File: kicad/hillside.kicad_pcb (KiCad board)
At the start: 2 copper layers, 136.6 x 97.9 mm, 83 parts, among them J1 Haptic, J2 TRRS, J3 Bat_Pos, J4 Bat_GND, K1 SW_Key, K10 SW_Key, K11 SW_Key, K12 SW_Key, K13 SW_Key, K14 SW_Key, K15 SW_Key, K16 SW_Key, K17 SW_Key, K18 SW_Key, K19 SW_Key, K2 SW_Key, K20 SW_Rotary, K21 SW_Key, K22 SW_Key, K23 SW_Key, K24 SW_Key, K3 SW_Key, K4 SW_Key, K5 SW_Key, K6 SW_Key, K7 SW_Key, K8 SW_Key, K9 SW_Key, SW1 Reset, SW2 SW_Power, U1 ProMicro_r

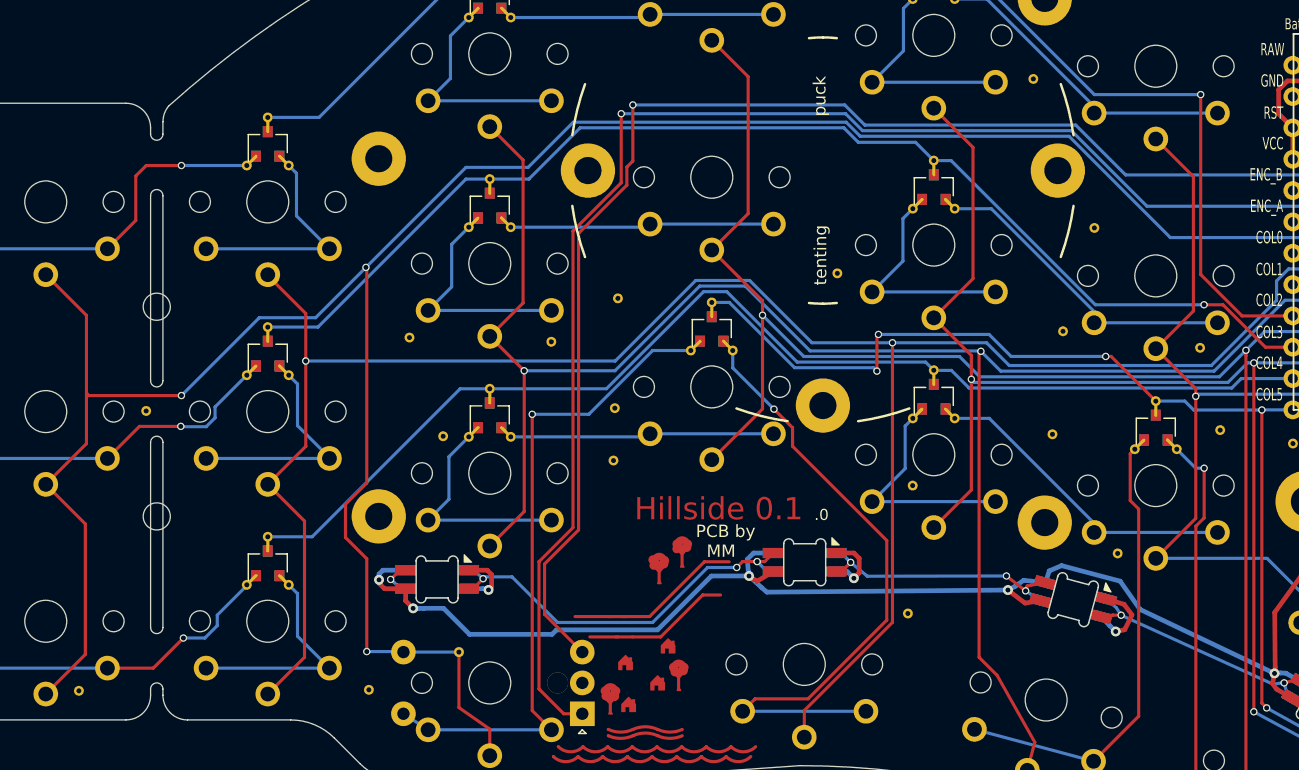
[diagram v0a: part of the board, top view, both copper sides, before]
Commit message: Remove stitching vias now handled by islands
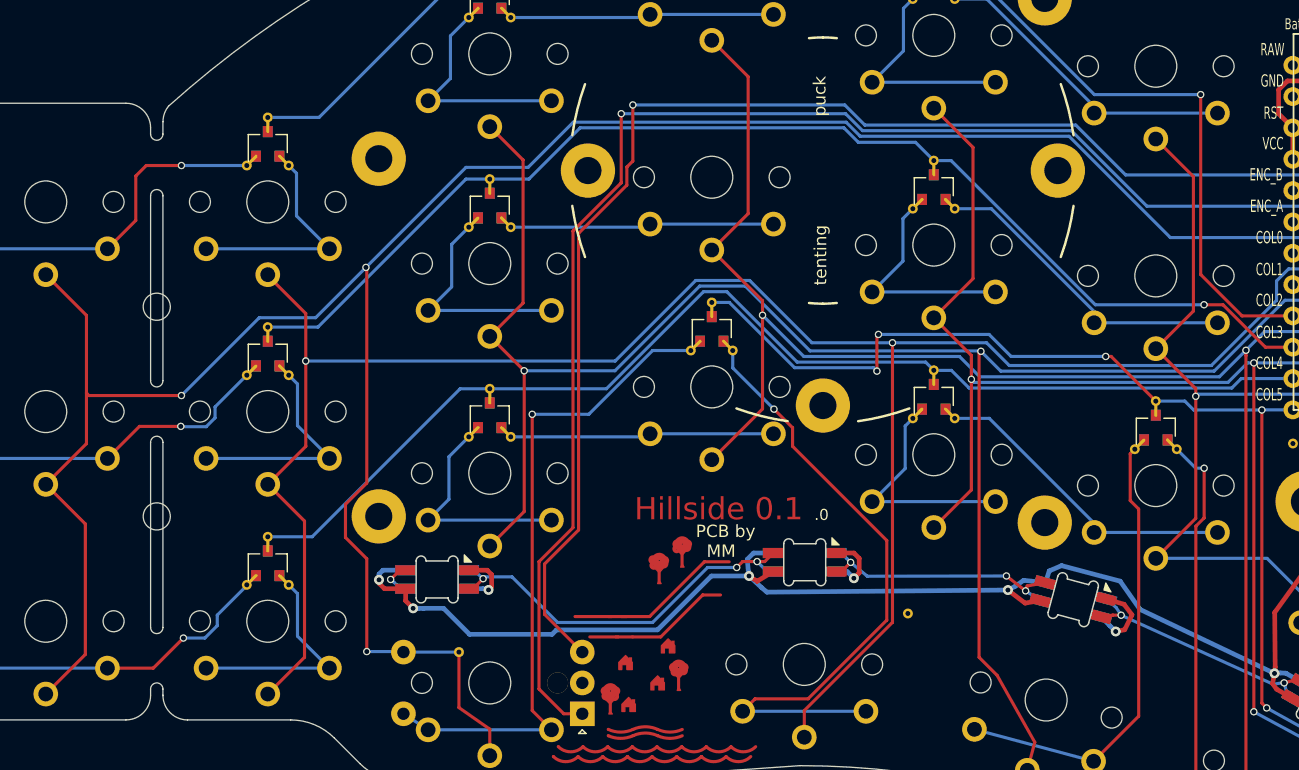
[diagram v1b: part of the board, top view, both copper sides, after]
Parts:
- removed V1, V10, V11, V12, V13, V14, V15, V16, V17, V18, V19, V20, V21, V22, V6, V7, V8, V9: Via, hillside_basic:VIA-0.8mm
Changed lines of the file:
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@@
       ))
-  )
-  (footprint "hillside_basic:VIA-0.8mm" (layer "F.Cu")
-    (at 146.03 105.47)
-    (attr through_hole)
-    (fp_text reference "V8" (at 1.3 1.4) (layer "F.Fab") hide
-      (effects (font (size 1 1) (thickness 0.15)))
-    )
-    (fp_text value "Via" (at -1.6 1.4) (layer "F.Fab") hide
-      (effects (font (size 1 1) (thickness 0.15)))
-    )
-    (pad "1" thru_hole circle locked (at 0 0) (size 0.8 0.8) (drill 0.4) (layers *.Cu)
-      (net 11 "GND") (zone_connect 2))
-  )
-  (footprint "hillside_basic:VIA-0.8mm" (layer "F.Cu")
-    (at 181.62 103.34)
-    (attr through_hole)
-    (fp_text reference "V9" (at 1.3 1.4) (layer "F.Fab") hide
-      (effects (font (size 1 1) (thickness 0.15)))
-    )
-    (fp_text value "Via" (at -1.6 1.4) (layer "F.Fab") hide
-      (effects (font (size 1 1) (thickness 0.15)))
-    )
-    (pad "1" thru_hole circle locked (at 0 0) (size 0.8 0.8) (drill 0.4) (layers *.Cu)
-      (net 11 "GND") (zone_connect 2))
-  )
-  (footprint "hillside_basic:VIA-0.8mm" (layer "F.Cu")
-    (at 126.2 124.06)
-    (attr through_hole)
-    (fp_text reference "V6" (at 1.3 1.4) (layer "F.Fab") hide
-      (effects (font (size 1 1) (thickness 0.15)))
-    )
-    (fp_text value "Via" (at -1.6 1.4) (layer "F.Fab") hide
-      (effects (font (size 1 1) (thickness 0.15)))
-    )
-    (pad "1" thru_hole circle locked (at 0 0) (size 0.8 0.8) (drill 0.4) (layers *.Cu)
-      (net 11 "GND") (zone_connect 2))
-  )
-  (footprint "hillside_basic:VIA-0.8mm" (layer "F.Cu")
-    (at 180.07 74.53)
-    (attr through_hole)
-    (fp_text reference "V1" (at 1.3 1.4) (layer "F.Fab") hide
-      (effects (font (size 1 1) (thickness 0.15)))
-    )
-    (fp_text value "Via" (at -1.6 1.4) (layer "F.Fab") hide
-      (effects (font (size 1 1) (thickness 0.15)))
-    )
-    (pad "1" thru_hole circle locked (at 0 0) (size 0.8 0.8) (drill 0.4) (layers *.Cu)
-      (net 11 "GND") (zone_connect 2))
-  )
-  (footprint "hillside_basic:VIA-0.8mm" (layer "F.Cu")
-    (at 146.39 92.32)
-    (attr through_hole)
-    (fp_text reference "V7" (at 1.3 1.4) (layer "F.Fab") hide
-      (effects (font (size 1 1) (thickness 0.15)))
-    )
-    (fp_text value "Via" (at -1.6 1.4) (layer "F.Fab") hide
-      (effects (font (size 1 1) (thickness 0.15)))
-    )
-    (pad "1" thru_hole circle locked (at 0 0) (size 0.8 0.8) (drill 0.4) (layers *.Cu)
-      (net 11 "GND") (zone_connect 2))
-  )
-  (footprint "hillside_basic:VIA-0.8mm" (layer "F.Cu")
-    (at 146.14 101.22)
-    (attr through_hole)
-    (fp_text reference "V10" (at 1.3 1.4) (layer "F.Fab") hide
-      (effects (font (size 1 1) (thickness 0.15)))
-    )
-    (fp_text value "Via" (at -1.6 1.4) (layer "F.Fab") hide
-      (effects (font (size 1 1) (thickness 0.15)))
-    )
-    (pad "1" thru_hole circle locked (at 0 0) (size 0.8 0.8) (drill 0.4) (layers *.Cu)
-      (net 11 "GND") (zone_connect 2))
-  )
-  (footprint "hillside_basic:VIA-0.8mm" (layer "F.Cu")
-    (at 182.48 94.99)
-    (attr through_hole)
-    (fp_text reference "V11" (at 1.3 1.4) (layer "F.Fab") hide
-      (effects (font (size 1 1) (thickness 0.15)))
-    )
-    (fp_text value "Via" (at -1.6 1.4) (layer "F.Fab") hide
-      (effects (font (size 1 1) (thickness 0.15)))
-    )
-    (pad "1" thru_hole circle locked (at 0 0) (size 0.8 0.8) (drill 0.4) (layers *.Cu)
-      (net 11 "GND") (zone_connect 2))
-  )
-  (footprint "hillside_basic:VIA-0.8mm" (layer "F.Cu")
-    (at 164.18 90.29)
-    (attr through_hole)
-    (fp_text reference "V12" (at 1.3 1.4) (layer "F.Fab") hide
-      (effects (font (size 1 1) (thickness 0.15)))
-    )
-    (fp_text value "Via" (at -1.6 1.4) (layer "F.Fab") hide
-      (effects (font (size 1 1) (thickness 0.15)))
-    )
-    (pad "1" thru_hole circle locked (at 0 0) (size 0.8 0.8) (drill 0.4) (layers *.Cu)
-      (net 11 "GND") (zone_connect 2))
-  )
-  (footprint "hillside_basic:VIA-0.8mm" (layer "F.Cu")
-    (at 129.49 95.5)
-    (attr through_hole)
-    (fp_text reference "V13" (at 1.3 1.4) (layer "F.Fab") hide
-      (effects (font (size 1 1) (thickness 0.15)))
-    )
-    (fp_text value "Via" (at -1.6 1.4) (layer "F.Fab") hide
-      (effects (font (size 1 1) (thickness 0.15)))
-    )
-    (pad "1" thru_hole circle locked (at 0 0) (size 0.8 0.8) (drill 0.4) (layers *.Cu)
-      (net 11 "GND") (zone_connect 2))
-  )
-  (footprint "hillside_basic:VIA-0.8mm" (layer "F.Cu")
-    (at 185.02 86.61)
-    (attr through_hole)
-    (fp_text reference "V14" (at 1.3 1.4) (layer "F.Fab") hide
-      (effects (font (size 1 1) (thickness 0.15)))
-    )
-    (fp_text value "Via" (at -1.6 1.4) (layer "F.Fab") hide
-      (effects (font (size 1 1) (thickness 0.15)))
-    )
-    (pad "1" thru_hole circle locked (at 0 0) (size 0.8 0.8) (drill 0.4) (layers *.Cu)
-      (net 11 "GND") (zone_connect 2))
-  )
-  (footprint "hillside_basic:VIA-0.8mm" (layer "F.Cu")
-    (at 102.69 124.14)
-    (attr through_hole)
-    (fp_text reference "V15" (at 1.3 1.4) (layer "F.Fab") hide
-      (effects (font (size 1 1) (thickness 0.15)))
-    )
-    (fp_text value "Via" (at -1.6 1.4) (layer "F.Fab") hide
-      (effects (font (size 1 1) (thickness 0.15)))
-    )
-    (pad "1" thru_hole circle locked (at 0 0) (size 0.8 0.8) (drill 0.4) (layers *.Cu)
-      (net 11 "GND") (zone_connect 2))
-  )
-  (footprint "hillside_basic:VIA-0.8mm" (layer "F.Cu")
-    (at 108.14 101.45)
-    (attr through_hole)
-    (fp_text reference "V16" (at 1.3 1.4) (layer "F.Fab") hide
-      (effects (font (size 1 1) (thickness 0.15)))
-    )
-    (fp_text value "Via" (at -1.6 1.4) (layer "F.Fab") hide
-      (effects (font (size 1 1) (thickness 0.15)))
-    )
-    (pad "1" thru_hole circle locked (at 0 0) (size 0.8 0.8) (drill 0.4) (layers *.Cu)
-      (net 11 "GND") (zone_connect 2))
-  )
-  (footprint "hillside_basic:VIA-0.8mm" (layer "F.Cu")
-    (at 195.22 103)
-    (attr through_hole)
-    (fp_text reference "V17" (at 1.3 1.4) (layer "F.Fab") hide
-      (effects (font (size 1 1) (thickness 0.15)))
-    )
-    (fp_text value "Via" (at -1.6 1.4) (layer "F.Fab") hide
-      (effects (font (size 1 1) (thickness 0.15)))
-    )
-    (pad "1" thru_hole circle locked (at 0 0) (size 0.8 0.8) (drill 0.4) (layers *.Cu)
-      (net 11 "GND") (zone_connect 2))
-  )
-  (footprint "hillside_basic:VIA-0.8mm" (layer "F.Cu")
-    (at 193.59 96.33)
-    (attr through_hole)
-    (fp_text reference "V18" (at 1.3 1.4) (layer "F.Fab") hide
-      (effects (font (size 1 1) (thickness 0.15)))
-    )
-    (fp_text value "Via" (at -1.6 1.4) (layer "F.Fab") hide
-      (effects (font (size 1 1) (thickness 0.15)))
-    )
-    (pad "1" thru_hole circle locked (at 0 0) (size 0.8 0.8) (drill 0.4) (layers *.Cu)
-      (net 11 "GND") (zone_connect 2))
-  )
-  (footprint "hillside_basic:VIA-0.8mm" (layer "F.Cu")
-    (at 140.99 95.84)
-    (attr through_hole)
-    (fp_text reference "V19" (at 1.3 1.4) (layer "F.Fab") hide
-      (effects (font (size 1 1) (thickness 0.15)))
-    )
-    (fp_text value "Via" (at -1.6 1.4) (layer "F.Fab") hide
-      (effects (font (size 1 1) (thickness 0.15)))
-    )
-    (pad "1" thru_hole circle locked (at 0 0) (size 0.8 0.8) (drill 0.4) (layers *.Cu)
-      (net 11 "GND") (zone_connect 2))
-  )
-  (footprint "hillside_basic:VIA-0.8mm" (layer "F.Cu")
-    (at 186.91 113)
-    (attr through_hole)
-    (fp_text reference "V20" (at 0 1.4) (layer "F.Fab") hide
-      (effects (font (size 1 1) (thickness 0.15)))
-    )
-    (fp_text value "Via" (at 0 -1.4) (layer "F.Fab") hide
-      (effects (font (size 1 1) (thickness 0.15)))
-    )
-    (pad "1" thru_hole circle locked (at 0 0) (size 0.8 0.8) (drill 0.4) (layers *.Cu)
-      (net 11 "GND") (zone_connect 2))
-  )
-  (footprint "hillside_basic:VIA-0.8mm" (layer "F.Cu")
-    (at 132.22 103.5)
-    (attr through_hole)
-    (fp_text reference "V21" (at 0 1.4) (layer "F.Fab") hide
-      (effects (font (size 1 1) (thickness 0.15)))
-    )
-    (fp_text value "Via" (at 0 -1.4) (layer "F.Fab") hide
-      (effects (font (size 1 1) (thickness 0.15)))
-    )
-    (pad "1" thru_hole circle locked (at 0 0) (size 0.8 0.8) (drill 0.4) (layers *.Cu)
-      (net 11 "GND") (zone_connect 2))
-  )
-  (footprint "hillside_basic:VIA-0.8mm" (layer "F.Cu")
-    (at 170.29 107.5)
-    (attr through_hole)
-    (fp_text reference "V22" (at 0 1.4) (layer "F.Fab") hide
-      (effects (font (size 1 1) (thickness 0.15)))
-    )
-    (fp_text value "Via" (at 0 -1.4) (layer "F.Fab") hide
-      (effects (font (size 1 1) (thickness 0.15)))
-    )
-    (pad "1" thru_hole circle locked (at 0 0) (size 0.8 0.8) (drill 0.4) (layers *.Cu)
-      (net 11 "GND") (zone_connect 2))
   )
   (footprint "hillside_basic:MountingHole_2.2mm_M2_Pad" (layer "F.Cu")
@@
     (connect_pads (clearance 0.508))
     (min_thickness 0.254) (filled_areas_thickness no)
-    (fill yes (thermal_gap 0.508) (thermal_bridge_width 0.508) (smoothing chamfer) (radius 1))
+    (fill yes (thermal_gap 0.508) (thermal_bridge_width 0.508) (smoothing chamfer) (radius 1) (island_removal_mode 2) (island_area_min 2))
     (polygon
       (pts
@@
     (connect_pads (clearance 0.508))
     (min_thickness 0.254) (filled_areas_thickness no)
-    (fill yes (thermal_gap 0.508) (thermal_bridge_width 0.508) (smoothing chamfer) (radius 1))
+    (fill yes (thermal_gap 0.508) (thermal_bridge_width 0.508) (smoothing chamfer) (radius 1) (island_removal_mode 2) (island_area_min 2))
     (polygon
       (pts

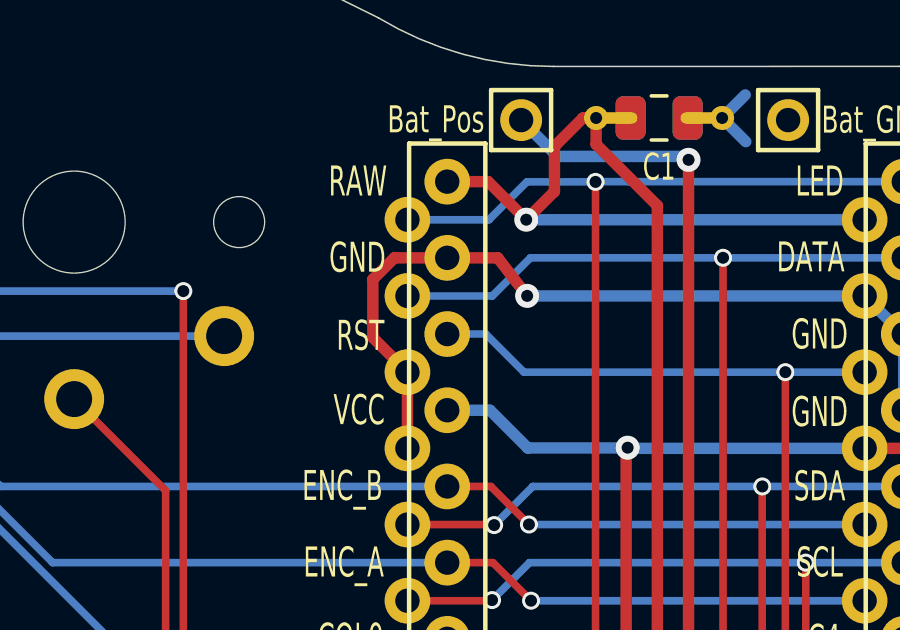
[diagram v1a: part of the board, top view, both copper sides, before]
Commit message: pcb: route GND inside MCU footprint
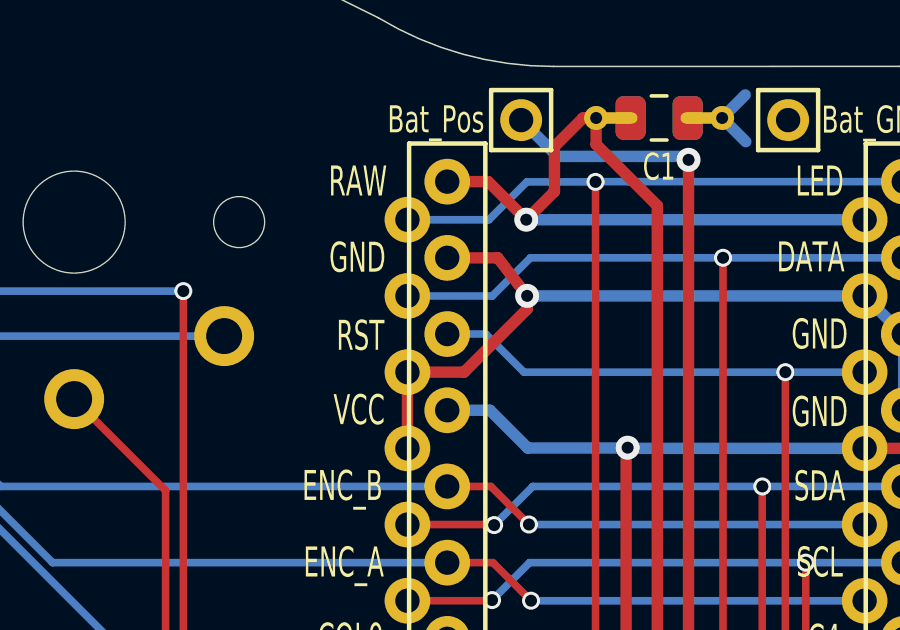
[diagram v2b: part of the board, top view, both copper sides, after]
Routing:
- net GND: track 57.5 -> 56.5 mm
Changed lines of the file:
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@@
   (segment (start 205.1 75.96) (end 204.122 74.692) (width 0.381) (layer "F.Cu") (net 11))
   (segment (start 135.790406 114.36) (end 134.28 114.36) (width 0.381) (layer "F.Cu") (net 11))
-  (segment (start 199.957499 75.408799) (end 199.957499 77.349499) (width 0.381) (layer "F.Cu") (net 11))
   (segment (start 186.75 119.33) (end 187.48 119.19) (width 0.381) (layer "F.Cu") (net 11))
+  (segment (start 202.998 78.502) (end 205.1 76.4) (width 0.381) (layer "F.Cu") (net 11))
   (segment (start 188.07 117.98) (end 187.425639 117.124361) (width 0.381) (layer "F.Cu") (net 11))
-  (segment (start 199.957499 77.349499) (end 201.11 78.502) (width 0.381) (layer "F.Cu") (net 11))
   (segment (start 187.48 119.19) (end 188.07 117.98) (width 0.381) (layer "F.Cu") (net 11))
   (segment (start 187.425639 117.124361) (end 185.960896 116.688311) (width 0.381) (layer "F.Cu") (net 11))
   (segment (start 204.122 74.692) (end 202.4364 74.692) (width 0.381) (layer "F.Cu") (net 11))
   (segment (start 136.149475 115.708678) (end 136.149475 114.719069) (width 0.381) (layer "F.Cu") (net 11))
+  (segment (start 205.1 76.4) (end 205.1 75.96) (width 0.381) (layer "F.Cu") (net 11))
   (segment (start 135.899076 115.959076) (end 136.149475 115.708678) (width 0.381) (layer "F.Cu") (net 11))
+  (segment (start 201.11 78.502) (end 202.998 78.502) (width 0.381) (layer "F.Cu") (net 11))
   (segment (start 136.149475 114.719069) (end 135.790406 114.36) (width 0.381) (layer "F.Cu") (net 11))
-  (segment (start 202.4364 74.692) (end 200.674298 74.692) (width 0.381) (layer "F.Cu") (net 11))
-  (segment (start 200.674298 74.692) (end 199.957499 75.408799) (width 0.381) (layer "F.Cu") (net 11))
   (segment (start 201.11 78.502) (end 201.11 81.042) (width 0.381) (layer "F.Cu") (net 11))
   (via (at 207.792123 127.71424) (size 0.8) (drill 0.4) (layers "F.Cu" "B.Cu") (net 11))
